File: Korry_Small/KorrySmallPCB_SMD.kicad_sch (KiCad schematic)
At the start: 9 parts, among them J1 BTN+LED, J2 BK_LED, SW1 SW

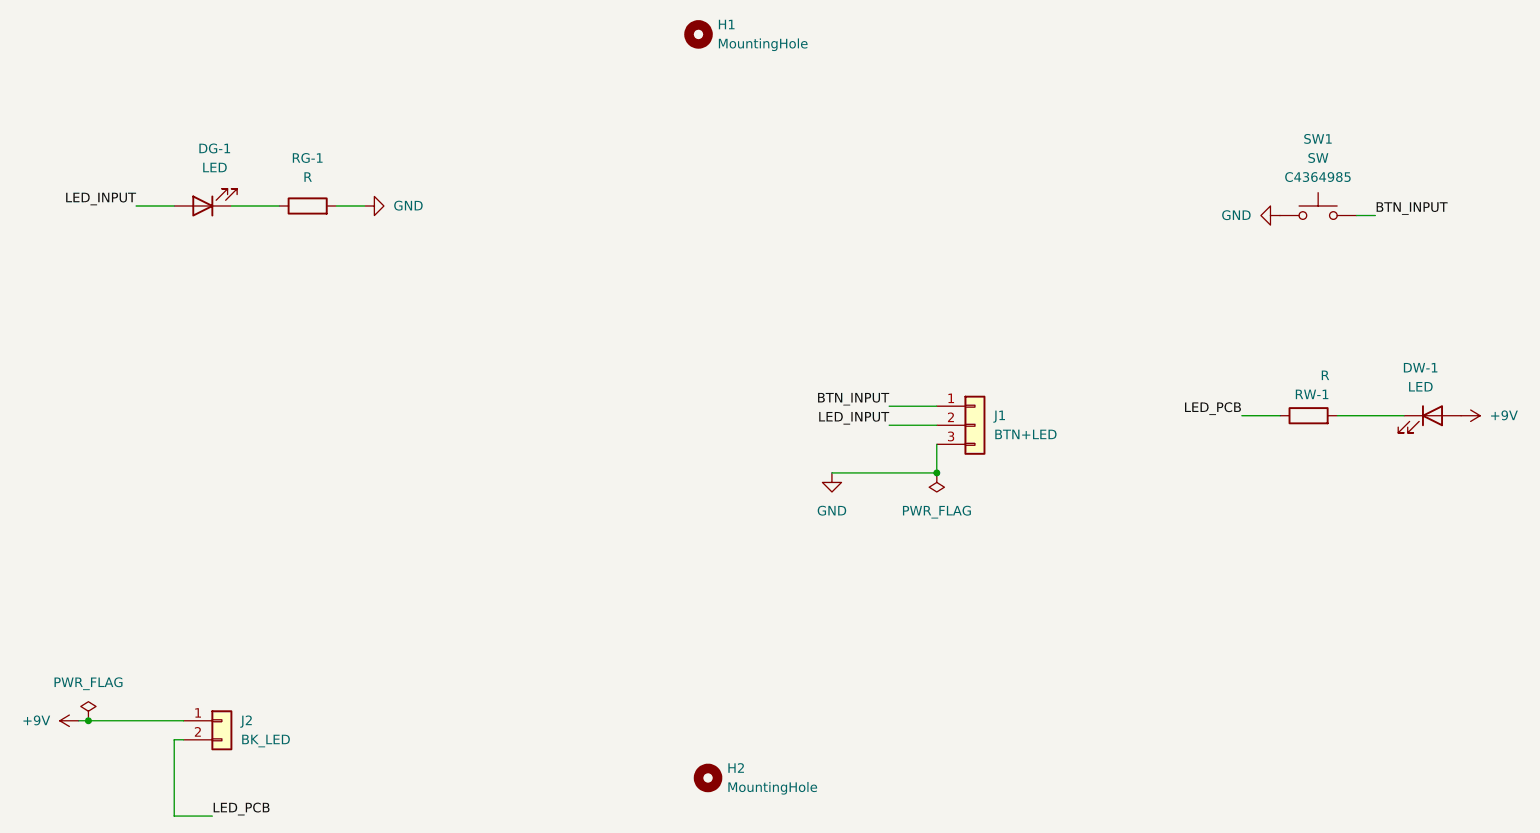
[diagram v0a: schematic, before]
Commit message: Fix the swapped EFIS filenames and rename the backlight nets to +5V
Two naming defects, no electrical change on any board.

EFIS sheets
-----------
The root sheet pointed EFIS_LEFT at efis_right.kicad_sch and EFIS_RIGHT at
efis_left.kicad_sch. The schematic was correct, since the file behind the
LEFT sheet did hold the L_* signals, but the filenames said the opposite and
anyone reading the files from outside KiCad would have been misled.

The two files are swapped and every reference follows: the sheet properties
in the root schematic and the 49 sheetfile entries the footprints carry on
the board. Each file now matches the sheet that loads it.

  netlist   198 nets, 135 components, not one node moved
  ERC       0 violations
  DRC       6 violations, all cosmetic, 0 unconnected, 0 parity issues

Backlight nets
--------------
Every net in the backlighting chain was called +9V while carrying 5 V, on
all four boards. The white LEDs sit behind 91 Ω: at 5 V that is 21 mA, right
at the rating for a 1206 white LED, while 9 V would put them at 65 mA. The
name was a leftover from an earlier design and was the kind of label that
eventually makes someone connect the wrong supply.

Renamed across Korry_Large, Korry_Small, Backlighting_Dimmer and
Backlighting_LEDModule, in both the schematics and the boards: the power
symbol, its value, which is what actually names the net, and the net entries
on the copper. 88 occurrences. None of those boards had a +5V net already,
so nothing was merged.

Verified against the state committed a moment ago: ERC and DRC counts are
identical on all four boards, before and after, and no board gained or lost
a connection.

The Readme drops these two entries and gains the defects that surfaced while
checking: the Backlighting_Dimmer footprints carry their reference in the
value field instead of the schematic value, so a BOM read from that board is
wrong; its terminal block footprint no longer exists in the KiCad library;
four texts on the Korry_Large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
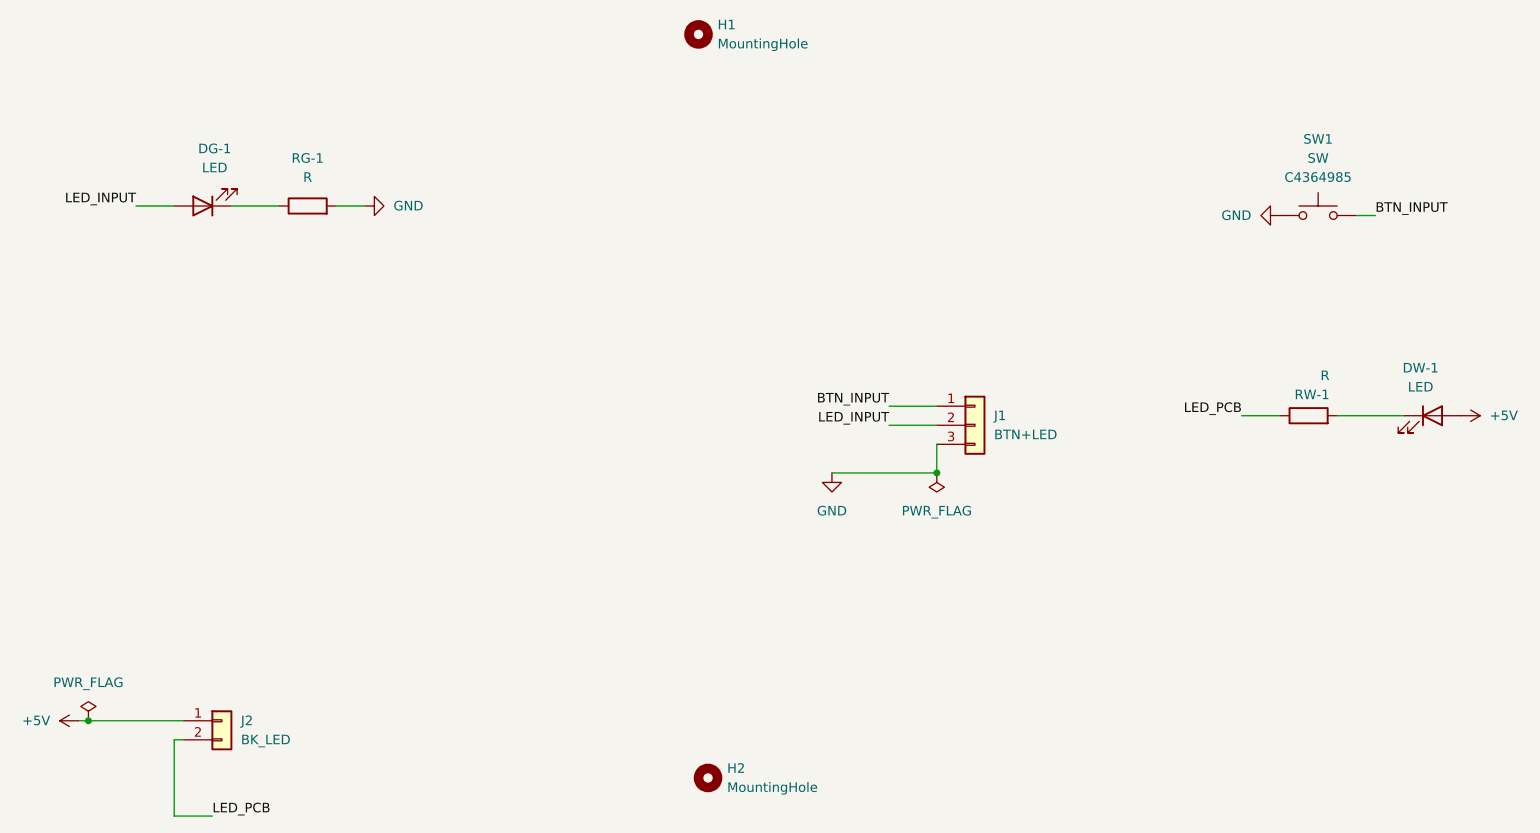
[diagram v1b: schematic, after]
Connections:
- net +9V renamed +5V
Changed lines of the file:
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@@
 	)
 	(symbol
-		(lib_id "power:+9V")
+		(lib_id "power:+5V")
 		(at 62.23 123.19 90)
 		(unit 1)
@@
 			)
 		)
-		(property "Value" "+9V"
+		(property "Value" "+5V"
 			(at 58.42 123.19 90)
 			(effects
@@
 	)
 	(symbol
-		(lib_id "power:+9V")
+		(lib_id "power:+5V")
 		(at 246.38 82.55 270)
 		(unit 1)
@@
 			)
 		)
-		(property "Value" "+9V"
+		(property "Value" "+5V"
 			(at 250.19 82.5499 90)
 			(effects

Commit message: Re-annotate the dimmer against its board, set the Korry resistor values
Tidying only. No board changed, no connection moved: all six projects still
report 0 unconnected items and 0 schematic parity issues.

Backlighting_Dimmer was worse than the value mismatch the Readme recorded.
Its schematic and its board disagreed on six reference designators, and
three separate connectors in the schematic all carried J73:

  J73 -> J12, J13, J14     three connectors sharing one reference
  J12 -> J31               J12 was the potentiometer in the schematic and a
                           terminal block on the board
  J93 -> J32
  U2  -> U1

Running Update PCB from Schematic on that board would have pushed those
references onto the copper and left three footprints called J73, against a
silkscreen that is already manufactured. The board is physical reality, so
the schematic was back-annotated from it, values included: R 5K became 5K,
C 470nF became 470nF and so on, which is also the better BOM text.
Schematic parity on that board goes from 6 to 0.

Backlighting_LEDModule had the same problem on one symbol, J73 -> J11.

The Korry resistors had no value in either schematic. Set to the fitted
parts, in the schematics and on the boards: RG 220 ohm for the green
annunciator, RW 91 ohm for the white backlight LED. At 5 V that is about
11 mA and 21 mA.

Three findings are deliberately left as they are, and the Readme now says
why rather than listing them as things to do:

- the dangling terminal block footprint has no replacement in KiCad 10,
  which ships no 2-pin 5.08 mm terminal block. Retargeting it would change
  the pads of a board already made
- the unmirrored + and - markers on the Korry_Large back silkscreen are
  symmetric glyphs, so nothing reads wrong, and mirroring them would move
  them sideways
- the PWR_FLAG the LEDModule wants is a two-click job in Eeschema. That
  file is KiCad 8 and the symbol definition would have to come from a
  KiCad 10 library carrying five toke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
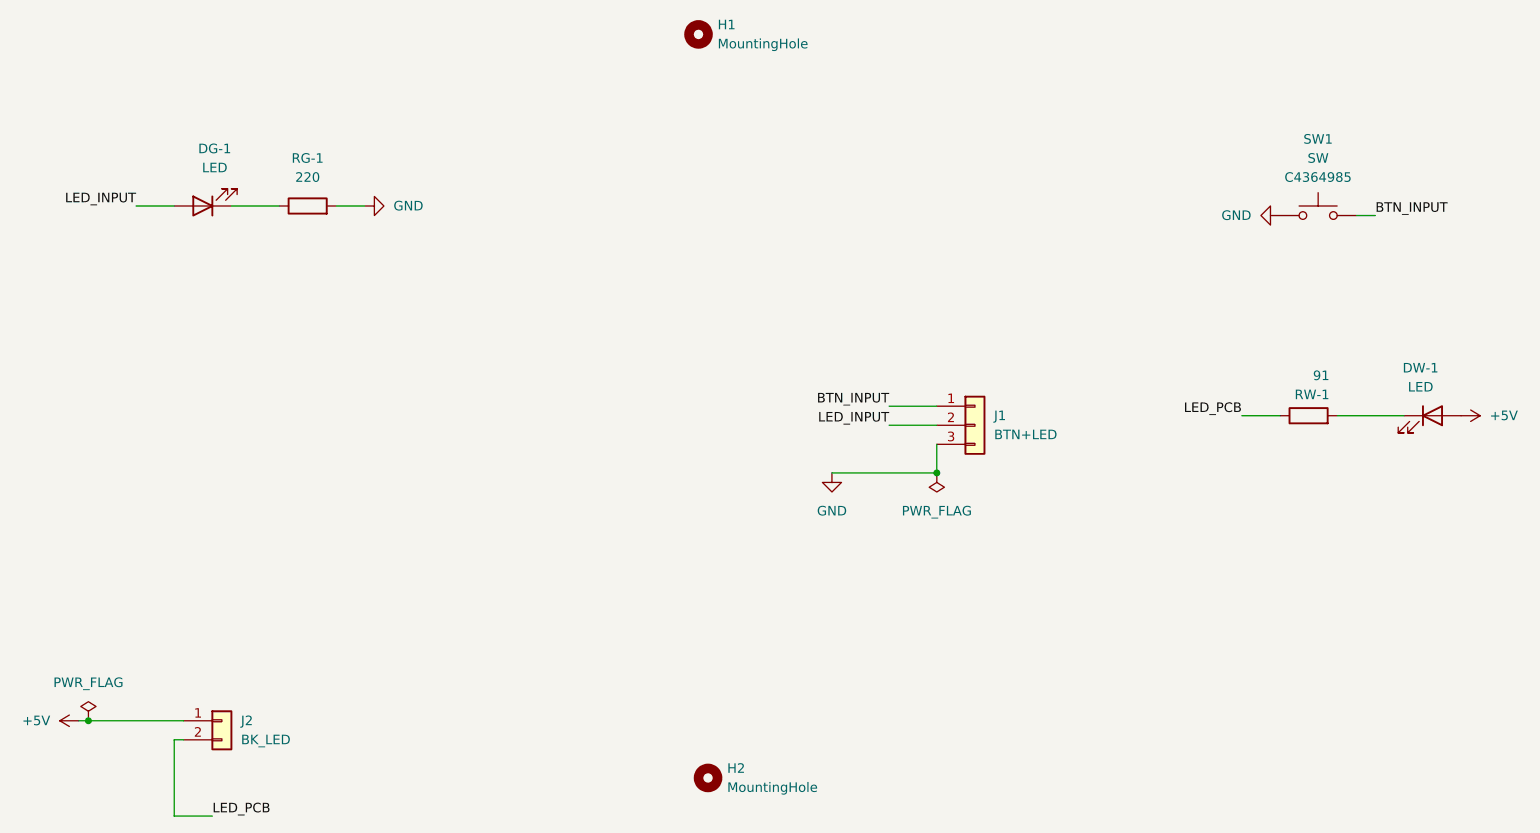
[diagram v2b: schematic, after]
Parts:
- RG-1: value R -> 220
- RW-1: value R -> 91
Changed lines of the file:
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@@
 			)
 		)
-		(property "Value" "R"
+		(property "Value" "220"
 			(at 92.71 50.8 90)
 			(effects
@@
 			)
 		)
-		(property "Value" "R"
+		(property "Value" "91"
 			(at 228.854 77.216 90)
 			(effects

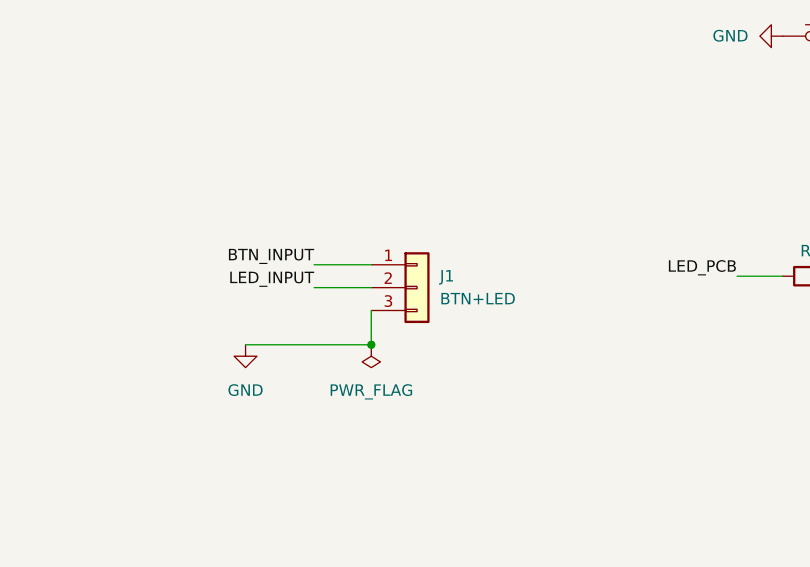
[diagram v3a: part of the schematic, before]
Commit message: Align the Korry connector with the mainboard
La mainboard mette GND sul pin 1 di tutti e 34 i suoi connettori a 3 pin. I
Korry avevano pin 1 = pulsante e pin 3 = GND, quindi con un cavetto dritto
la massa finiva sull'ingresso del pulsante e l'ingresso del multiplexer
sulla massa del Korry. Funzionava solo infilando il connettore al
contrario.

Scambiati i pin 1 e 3 sul Korry, che ha un connettore per scheda, e non
sulla mainboard, che ne ha venti e che con GND sul pin 1 e' coerente con se
stessa.

Sullo schema il simbolo di J1 e' specchiato sull'asse X: i pin 1 e 3 si
scambiano di posto e i fili che c'erano finiscono da soli su quello giusto.
Sul rame si sono scambiate le reti dei due pad e si e' rifatta la pista del
pulsante, che ora esce dall'altro capo del connettore; la massa la prende il
piano come prima. Sul Korry grande la pista scansa il pad 3 dello switch,
che e' massa e sta in mezzo.

Scambiate anche le lettere 'G' e 'B' sul serigrafico, che indicano i pin e
sarebbero diventate bugiarde.

Netlist verificata: J1 ora e' 1=GND, 2=LED_INPUT, 3=BTN_INPUT su entrambe.
Le zone sono da riempire.

Co-Authored-By: Claude Opus 5 <noreply@anthropic.com>
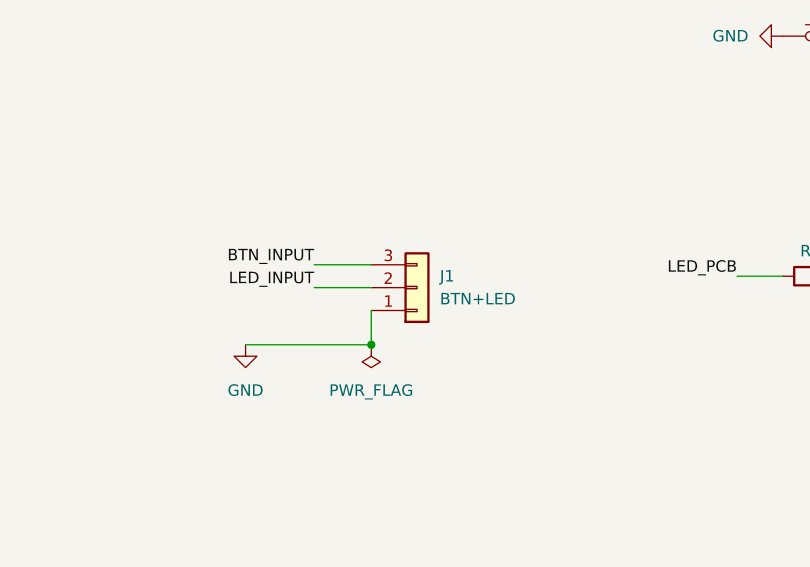
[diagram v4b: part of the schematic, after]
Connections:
- net BTN_INPUT: now also J1.3 (Pin_3); no longer J1.1 (Pin_1)
- net GND: now also J1.1 (Pin_1); no longer J1.3 (Pin_3)
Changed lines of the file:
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@@
 		(lib_id "Connector_Generic:Conn_01x03")
 		(at 181.61 83.82 0)
+		(mirror x)
 		(unit 1)
 		(body_style 1)
